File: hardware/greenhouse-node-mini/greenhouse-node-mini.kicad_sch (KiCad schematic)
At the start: 40 parts, among them J1 Molex_KK_396_1x2, J2 JST_XH_2.54mm_1x2, J3 Conn_01x05_Female, J4 Molex_KK_396_1x2, J5 JST_XH_2.54mm_1x4, SW1 SW_Push, U1 ATtiny84A-P, U2 L7805, U3 PCF8574, U4 L298HN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

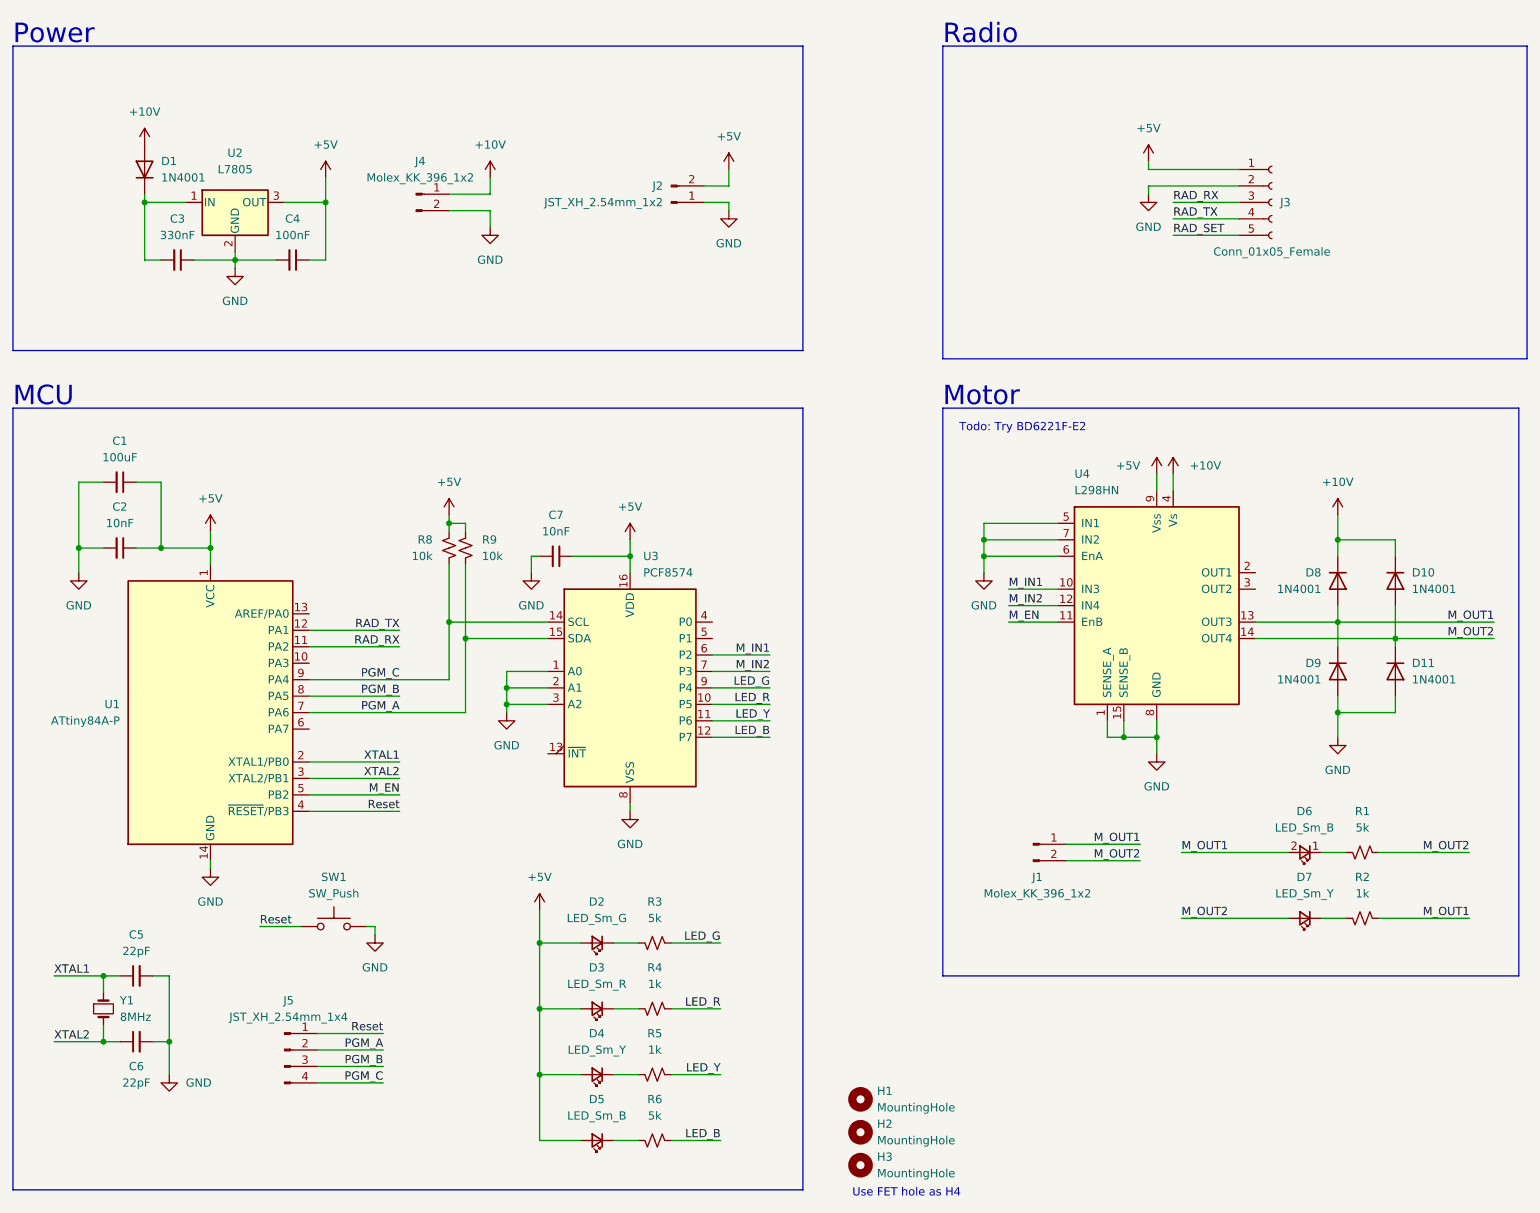
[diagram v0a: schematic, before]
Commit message: Moved voltage drop to nodes
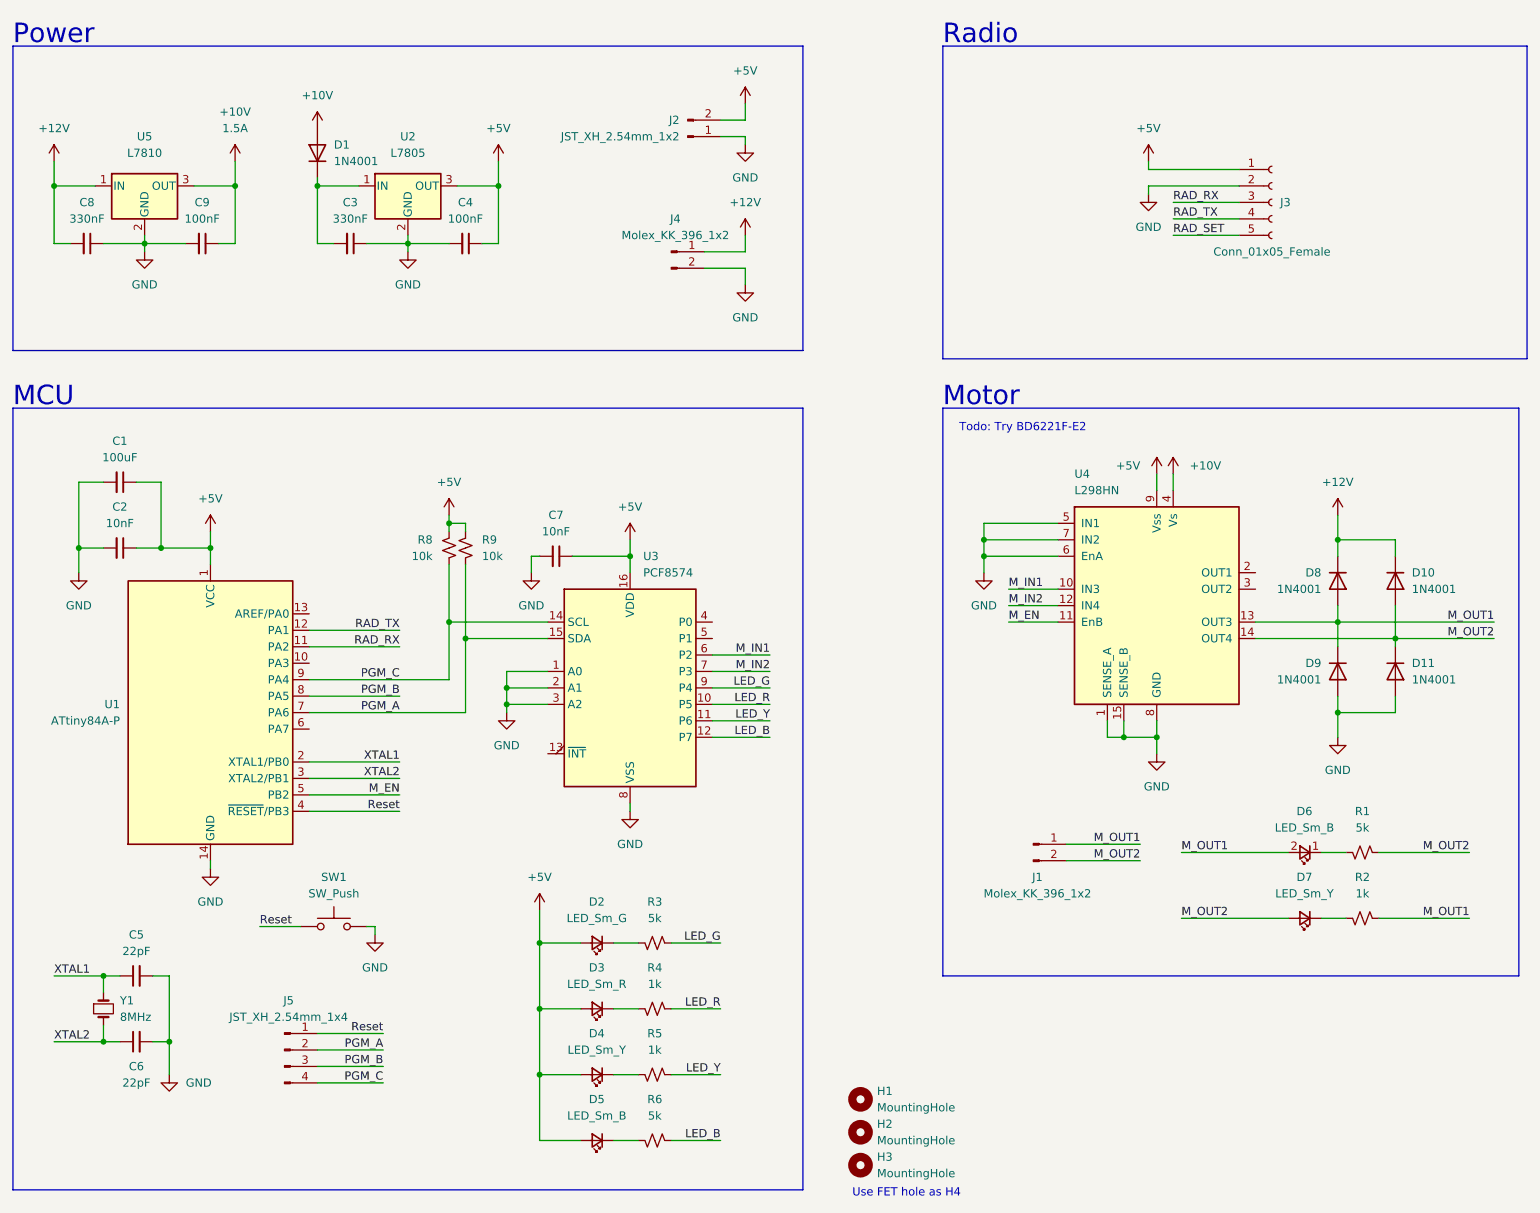
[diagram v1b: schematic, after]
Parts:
- added C8: 330nF, Capacitor_THT:C_Disc_D4.7mm_W2.5mm_P5.00mm, symbol Device:C_Small
- added C9: 100nF, Capacitor_THT:C_Disc_D4.7mm_W2.5mm_P5.00mm, symbol Device:C_Small
- added U5: L7810, Package_TO_SOT_THT:TO-220-3_Vertical, symbol Regulator_Linear:L7805
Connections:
- net +10V: now also C9.1, U5.3 (OUT); no longer D10.1 (K), D8.1 (K), J4.1 (Pin_1)
- net GND: now also C8.1, C9.2, U5.2 (GND)
- new net +12V: C8.2, D10.1 (K), D8.1 (K), J4.1 (Pin_1), U5.1 (IN)
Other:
- moved on the sheet: C3, C4, D1, J2, J4, U2

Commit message: Final changes for fab/prod
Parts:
- R1, R2, R3, R4, R5, R6, R8, R9: footprint Resistor_THT:R_Axial_DIN0204_L3.6mm_D1.6mm_P7.62mm_Horizontal -> Resistor_THT:R_Axial_DIN0207_L6.3mm_D2.5mm_P7.62mm_Horizontal
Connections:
- net M_OUT1: now also J1.2 (Pin_2); no longer J1.1 (Pin_1)
- net M_OUT2: now also J1.1 (Pin_1); no longer J1.2 (Pin_2)
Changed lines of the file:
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@@
     (effects (font (size 1.27 1.27)) (justify left bottom))
-  )
-  (label "M_OUT2" (at 200.66 144.78 180)
-    (effects (font (size 1.27 1.27)) (justify right bottom))
   )
   (label "M_OUT1" (at 251.46 153.67 180)
@@
     (effects (font (size 1.27 1.27)) (justify right bottom))
   )
-  (label "M_OUT1" (at 200.66 142.24 180)
+  (label "M_OUT1" (at 200.66 144.78 180)
     (effects (font (size 1.27 1.27)) (justify right bottom))
   )
@@
   )
   (label "PGM_B" (at 86.36 119.38 180)
+    (effects (font (size 1.27 1.27)) (justify right bottom))
+  )
+  (label "M_OUT2" (at 200.66 142.24 180)
     (effects (font (size 1.27 1.27)) (justify right bottom))
   )
@@
       (effects (font (size 1.27 1.27)) (justify left))
     )
-    (property "Footprint" "Resistor_THT:R_Axial_DIN0204_L3.6mm_D1.6mm_P7.62mm_Horizontal" (id 2) (at 93.98 96.52 0)
+    (property "Footprint" "Resistor_THT:R_Axial_DIN0207_L6.3mm_D2.5mm_P7.62mm_Horizontal" (id 2) (at 93.98 96.52 0)
       (effects (font (size 1.27 1.27)) hide)
     )
@@
     (property "Reference" "R4" (id 0) (at 125.73 161.29 90))
     (property "Value" "1k" (id 1) (at 125.73 163.83 90))
-    (property "Footprint" "Resistor_THT:R_Axial_DIN0204_L3.6mm_D1.6mm_P7.62mm_Horizontal" (id 2) (at 125.73 167.64 0)
+    (property "Footprint" "Resistor_THT:R_Axial_DIN0207_L6.3mm_D2.5mm_P7.62mm_Horizontal" (id 2) (at 125.73 167.64 0)
       (effects (font (size 1.27 1.27)) hide)
     )
@@
       (effects (font (size 1.27 1.27)) (justify right))
     )
-    (property "Footprint" "Resistor_THT:R_Axial_DIN0204_L3.6mm_D1.6mm_P7.62mm_Horizontal" (id 2) (at 96.52 96.52 0)
+    (property "Footprint" "Resistor_THT:R_Axial_DIN0207_L6.3mm_D2.5mm_P7.62mm_Horizontal" (id 2) (at 96.52 96.52 0)
       (effects (font (size 1.27 1.27)) hide)
     )
@@
     (property "Reference" "R6" (id 0) (at 125.73 181.61 90))
     (property "Value" "5k" (id 1) (at 125.73 184.15 90))
-    (property "Footprint" "Resistor_THT:R_Axial_DIN0204_L3.6mm_D1.6mm_P7.62mm_Horizontal" (id 2) (at 125.73 187.96 0)
+    (property "Footprint" "Resistor_THT:R_Axial_DIN0207_L6.3mm_D2.5mm_P7.62mm_Horizontal" (id 2) (at 125.73 187.96 0)
       (effects (font (size 1.27 1.27)) hide)
     )
@@
     (property "Reference" "R3" (id 0) (at 125.73 151.13 90))
     (property "Value" "5k" (id 1) (at 125.73 153.67 90))
-    (property "Footprint" "Resistor_THT:R_Axial_DIN0204_L3.6mm_D1.6mm_P7.62mm_Horizontal" (id 2) (at 125.73 157.48 0)
+    (property "Footprint" "Resistor_THT:R_Axial_DIN0207_L6.3mm_D2.5mm_P7.62mm_Horizontal" (id 2) (at 125.73 157.48 0)
       (effects (font (size 1.27 1.27)) hide)
     )
@@
     (property "Reference" "R5" (id 0) (at 125.73 171.45 90))
     (property "Value" "1k" (id 1) (at 125.73 173.99 90))
-    (property "Footprint" "Resistor_THT:R_Axial_DIN0204_L3.6mm_D1.6mm_P7.62mm_Horizontal" (id 2) (at 125.73 177.8 0)
+    (property "Footprint" "Resistor_THT:R_Axial_DIN0207_L6.3mm_D2.5mm_P7.62mm_Horizontal" (id 2) (at 125.73 177.8 0)
       (effects (font (size 1.27 1.27)) hide)
     )
@@
     (property "Reference" "R2" (id 0) (at 234.95 147.32 90))
     (property "Value" "1k" (id 1) (at 234.95 149.86 90))
-    (property "Footprint" "Resistor_THT:R_Axial_DIN0204_L3.6mm_D1.6mm_P7.62mm_Horizontal" (id 2) (at 234.95 153.67 0)
+    (property "Footprint" "Resistor_THT:R_Axial_DIN0207_L6.3mm_D2.5mm_P7.62mm_Horizontal" (id 2) (at 234.95 153.67 0)
       (effects (font (size 1.27 1.27)) hide)
     )
@@
     (property "Reference" "R1" (id 0) (at 234.95 137.16 90))
     (property "Value" "5k" (id 1) (at 234.95 139.7 90))
-    (property "Footprint" "Resistor_THT:R_Axial_DIN0204_L3.6mm_D1.6mm_P7.62mm_Horizontal" (id 2) (at 234.95 143.51 0)
+    (property "Footprint" "Resistor_THT:R_Axial_DIN0207_L6.3mm_D2.5mm_P7.62mm_Horizontal" (id 2) (at 234.95 143.51 0)
       (effects (font (size 1.27 1.27)) hide)
     )
@@
     )
     (path "/eb8c4f77-d931-4888-a754-0b09c6b8907f"
-      (reference "R1") (unit 1) (value "5k") (footprint "Resistor_THT:R_Axial_DIN0204_L3.6mm_D1.6mm_P7.62mm_Horizontal")
+      (reference "R1") (unit 1) (value "5k") (footprint "Resistor_THT:R_Axial_DIN0207_L6.3mm_D2.5mm_P7.62mm_Horizontal")
     )
     (path "/b6456347-a8b0-4beb-be5d-c94cb7d030d6"
-      (reference "R2") (unit 1) (value "1k") (footprint "Resistor_THT:R_Axial_DIN0204_L3.6mm_D1.6mm_P7.62mm_Horizontal")
+      (reference "R2") (unit 1) (value "1k") (footprint "Resistor_THT:R_Axial_DIN0207_L6.3mm_D2.5mm_P7.62mm_Horizontal")
     )
     (path "/8d8e4c38-c484-4fac-a511-73eabc76600a"
-      (reference "R3") (unit 1) (value "5k") (footprint "Resistor_THT:R_Axial_DIN0204_L3.6mm_D1.6mm_P7.62mm_Horizontal")
+      (reference "R3") (unit 1) (value "5k") (footprint "Resistor_THT:R_Axial_DIN0207_L6.3mm_D2.5mm_P7.62mm_Horizontal")
     )
     (path "/5e0eae24-dbad-48fb-ae7c-f6a4c82246b4"
-      (reference "R4") (unit 1) (value "1k") (footprint "Resistor_THT:R_Axial_DIN0204_L3.6mm_D1.6mm_P7.62mm_Horizontal")
+      (reference "R4") (unit 1) (value "1k") (footprint "Resistor_THT:R_Axial_DIN0207_L6.3mm_D2.5mm_P7.62mm_Horizontal")
     )
     (path "/aaf12300-f95b-4fd6-9598-8426feadbf1b"
-      (reference "R5") (unit 1) (value "1k") (footprint "Resistor_THT:R_Axial_DIN0204_L3.6mm_D1.6mm_P7.62mm_Horizontal")
+      (reference "R5") (unit 1) (value "1k") (footprint "Resistor_THT:R_Axial_DIN0207_L6.3mm_D2.5mm_P7.62mm_Horizontal")
     )
     (path "/8d8a3be9-1e0c-4839-a01e-a19d5822dac7"
-      (reference "R6") (unit 1) (value "5k") (footprint "Resistor_THT:R_Axial_DIN0204_L3.6mm_D1.6mm_P7.62mm_Horizontal")
+      (reference "R6") (unit 1) (value "5k") (footprint "Resistor_THT:R_Axial_DIN0207_L6.3mm_D2.5mm_P7.62mm_Horizontal")
     )
     (path "/23299cf6-a16e-430c-ae20-6a5e83dd3ba0"
-      (reference "R8") (unit 1) (value "10k") (footprint "Resistor_THT:R_Axial_DIN0204_L3.6mm_D1.6mm_P7.62mm_Horizontal")
+      (reference "R8") (unit 1) (value "10k") (footprint "Resistor_THT:R_Axial_DIN0207_L6.3mm_D2.5mm_P7.62mm_Horizontal")
     )
     (path "/85534442-588d-49db-a19b-8db2c032d0fc"
-      (reference "R9") (unit 1) (value "10k") (footprint "Resistor_THT:R_Axial_DIN0204_L3.6mm_D1.6mm_P7.62mm_Horizontal")
+      (reference "R9") (unit 1) (value "10k") (footprint "Resistor_THT:R_Axial_DIN0207_L6.3mm_D2.5mm_P7.62mm_Horizontal")
     )
     (path "/50676101-d186-402b-b842-660a80bb31e9"
